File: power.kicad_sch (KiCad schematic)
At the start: 58 parts, among them J3 Conn_01x01, J4 Conn_01x01, U3 TPS53647, U36 MCP1824T-1202E, U6 AP3211, U7 MCP1824T-0802E

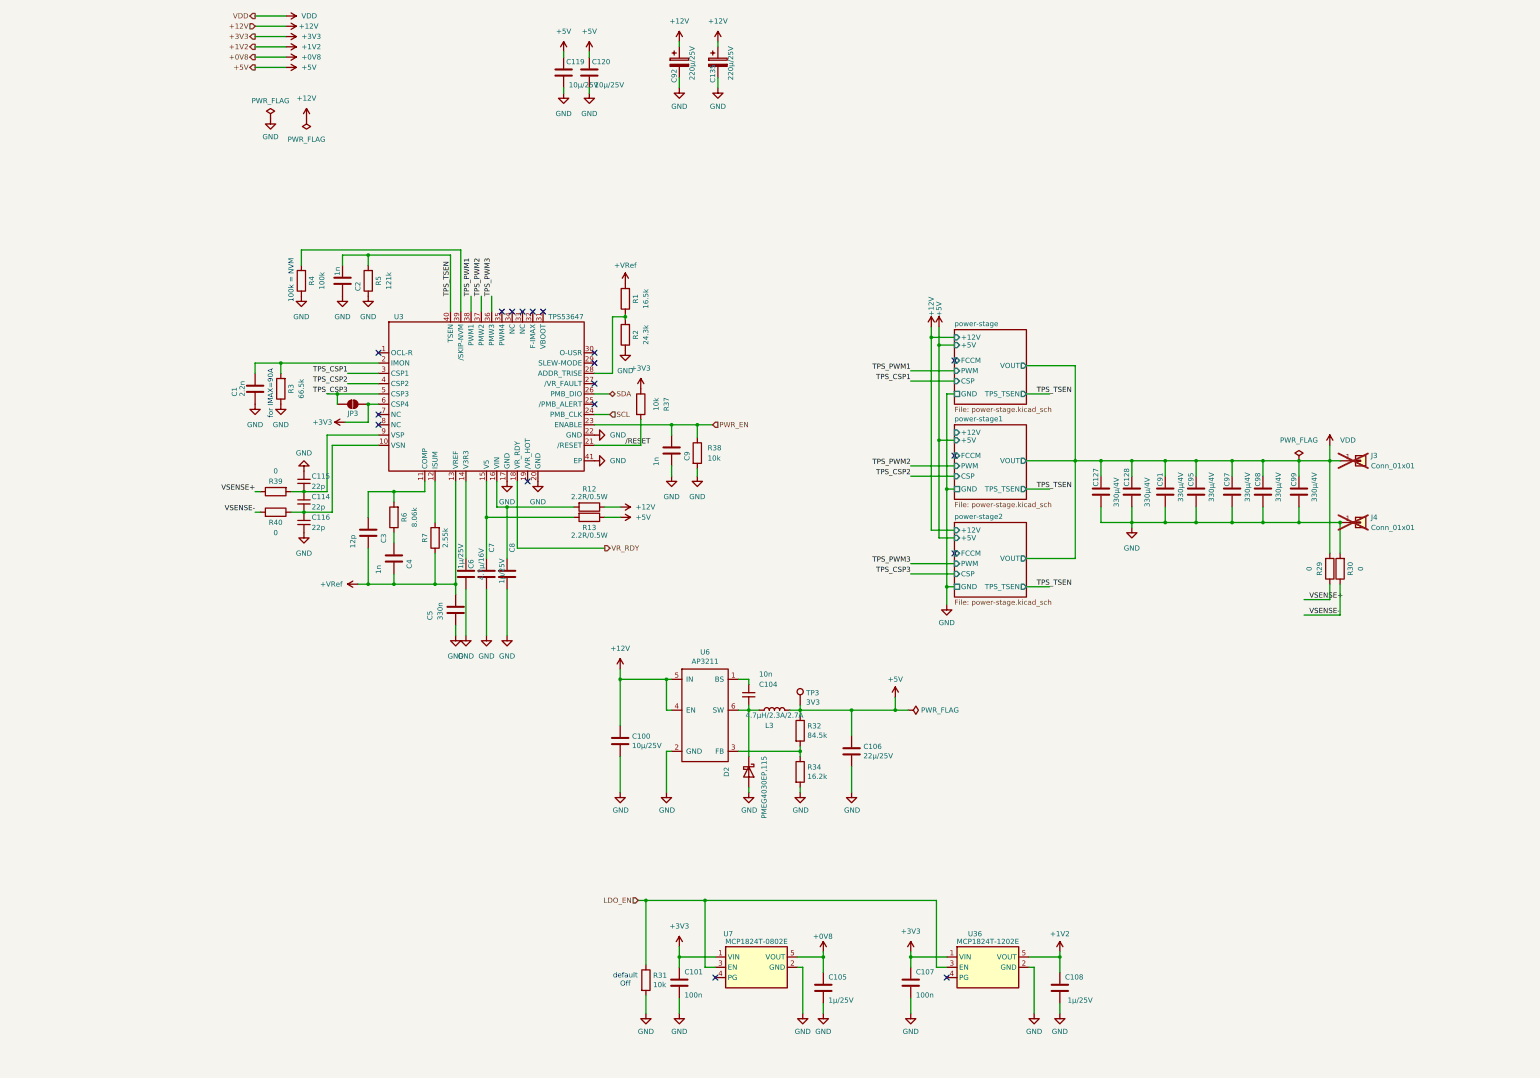
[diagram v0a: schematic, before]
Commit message: updated power stage placements
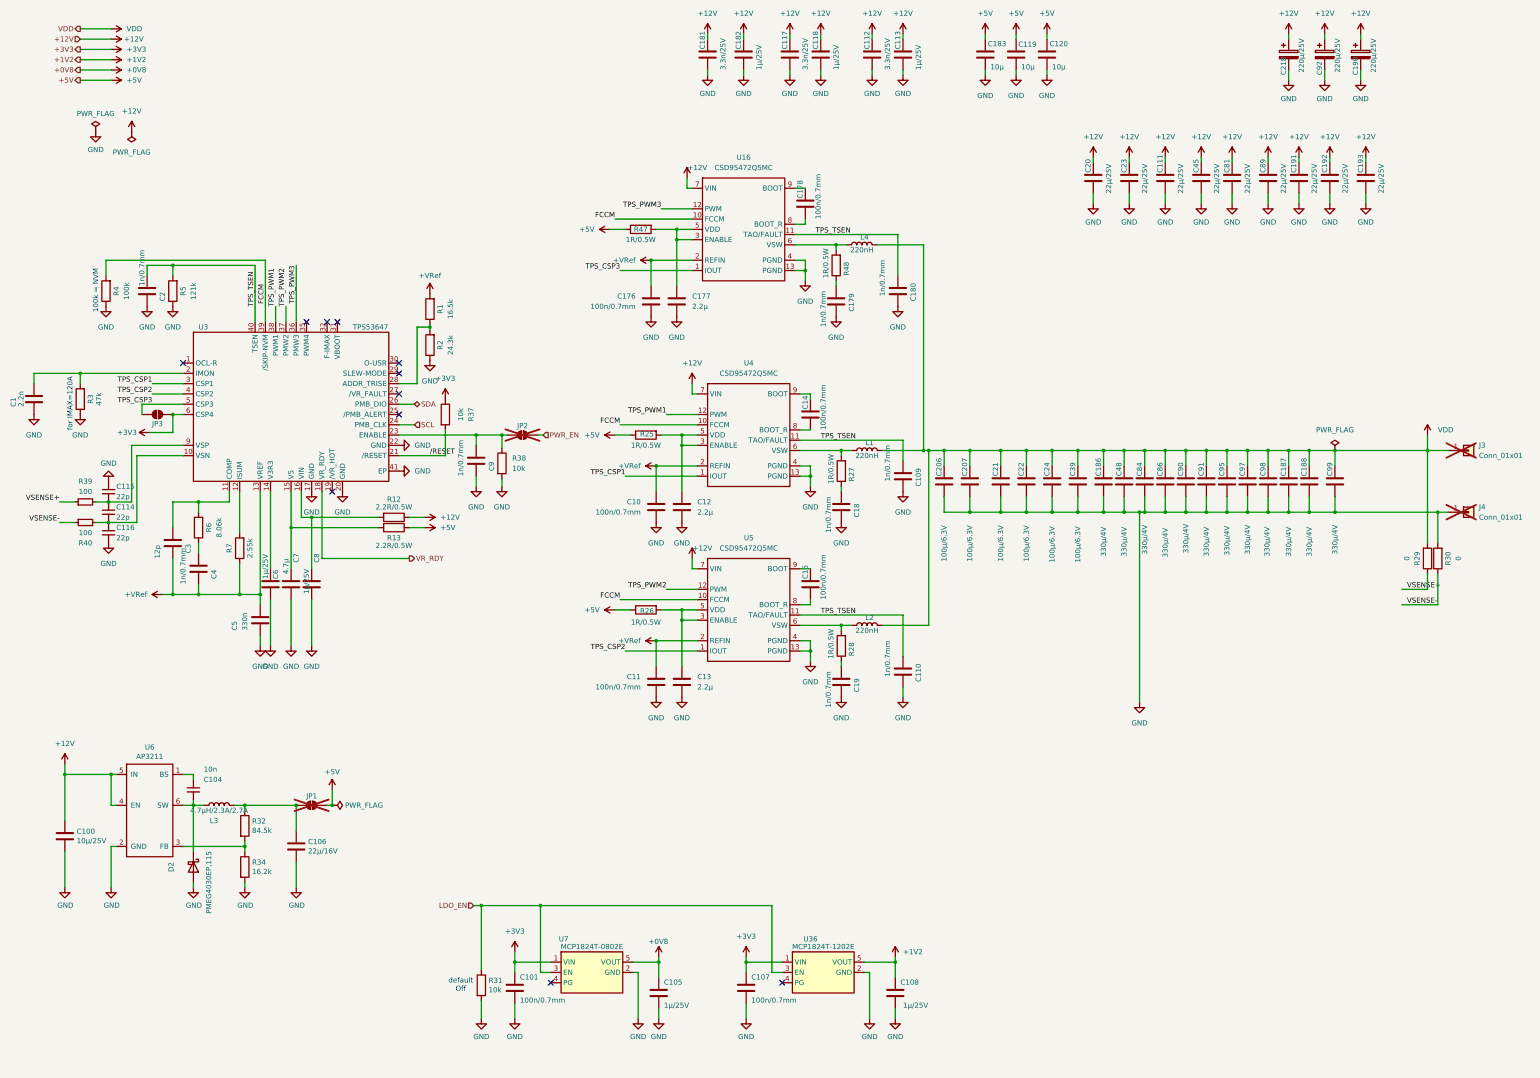
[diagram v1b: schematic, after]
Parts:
- removed C127, C128: 330µ/4V, Capacitor_SMD:C_1210_3225Metric, symbol Device:C
- removed C135: 220µ/25V, Capacitor_SMD:CP_Elec_8x10, symbol Device:C_Polarized
- removed R39, R40: 0, Resistor_SMD:R_0805_2012Metric, symbol Device:R
- removed TP3: 3V3, TestPoint:TestPoint_Pad_2.0x2.0mm, symbol Connector:TestPoint
- added C10, C11, C14, C16, C176, C178: 100n/0.7mm, Capacitor_SMD:C_0805_2012Metric, symbol Device:C
- added C109, C110, C179, C18, C180, C19: 1n/0.7mm, Capacitor_SMD:C_0805_2012Metric, symbol Device:C
- added C111, C191, C192, C193, C20, C23, C45, C81, C89: 22µ/25V, Capacitor_SMD:C_1210_3225Metric, symbol Device:C
- added C112, C117, C181: 3.3n/25V, Capacitor_SMD:C_0805_2012Metric, symbol Device:C
- added C113, C118, C182: 1µ/25V, Capacitor_SMD:C_0805_2012Metric, symbol Device:C
- added C12, C13, C177: 2.2µ, Capacitor_SMD:C_0805_2012Metric, symbol Device:C
- added C183: 10µ, Capacitor_SMD:C_0805_2012Metric, symbol Device:C
- added C186, C187, C188, C48, C84, C86, C90: 330µ/4V, Capacitor_SMD:C_1210_3225Metric, symbol Device:C
- added C190, C218: 220µ/25V, Capacitor_SMD:CP_Elec_8x10, symbol Device:C_Polarized
- added C206, C207, C21, C22, C24, C39: 100µ/6.3V, Capacitor_SMD:C_1210_3225Metric, symbol Device:C
- added JP1, JP2: SolderJumper_2_Open, Jumper:SolderJumper-2_P1.3mm_Open_RoundedPad1.0x1.5mm, symbol Jumper:SolderJumper_2_Open
- added L1, L2, L4: 220nH, Nerd8:IFLR-4031GC-01-8x10, symbol Device:L
- added R25, R26, R27, R28, R47, R48: 1R/0.5W, Resistor_SMD:R_0805_2012Metric, symbol Device:R
- added R39, R40: 100, Resistor_SMD:R_0805_2012Metric, symbol Device:R_Small
- added U16, U4, U5: CSD95472Q5MC, Nerd8:CSD95472-SON-5x6, symbol mylib7:CSD95472Q5MC
- C1: Manufacturer C0805C222J2GACTU -> CL21C222JBFNNNE; OrderNr 399-17628-1-ND -> 1276-2993-1-ND; temp-coefficient C0G -> (none)
- C100: Manufacturer GRM21BZ71E106KE15L -> C2012X5R1E106K125AB; OrderNr 490-GRM21BZ71E106KE15LCT-ND -> 445-5984-1-ND; temp-coefficient X7R -> (none)
- C101, C107: value 100n -> 100n/0.7mm; Manufacturer C0805C104K5RACTU -> AC0805KRX7R9BB104; OrderNr 399-C0805C104K5RACTUCT-ND -> 311-3037-1-ND; temp-coefficient X7R -> (none)
- C104: Manufacturer C0805C103J1GECTU -> 885012207011; OrderNr 399-C0805C103J1GECTUCT-ND -> 732-8021-1-ND; temp-coefficient C0G -> (none)
- C105, C108, C6, C8: Manufacturer CL21B105KBFNNNE -> CL21B105KAFNNNE; OrderNr 1276-1029-1-ND -> 1276-1066-1-ND; temp-coefficient X7R -> (none)
- C106: value 22µ/25V -> 22µ/16V; footprint Capacitor_SMD:C_1210_3225Metric -> Capacitor_SMD:C_1206_3216Metric; Manufacturer CL32B226KAJNNNE -> CL31A226MOCLNNC; OrderNr 1276-3392-1-ND -> 1276-2728-1-ND; temp-coefficient X7R -> (none)
- C114, C115, C116: OrderNr KGM15ACG1H220JT -> 478-KGM15ACG1H220JTCT-ND; temp-coefficient C0G -> (none)
- C119, C120: value 10µ/25V -> 10µ; Manufacturer GRM21BZ71E106KE15L -> C2012X5R1E106K125AB; OrderNr 490-GRM21BZ71E106KE15LCT-ND -> 445-5984-1-ND; temp-coefficient X7R -> (none)
- C2, C4, C9: value 1n -> 1n/0.7mm; Manufacturer C0805C102J2GECTU -> CC0805KRX7R0BB102; OrderNr 399-C0805C102J2GECTUCT-ND -> 311-1472-1-ND; temp-coefficient C0G -> (none)
- C3: OrderNr KGM15ACG2A120JM -> 478-KGM15ACG2A120JMCT-ND; temp-coefficient C0G -> (none)
- C5: Manufacturer CL21B334KBFNNNE -> C0805C334K3RECAUTO; OrderNr 1276-1123-1-ND -> 399-C0805C334K3RECAUTOCT-ND; temp-coefficient X7R -> (none)
- C7: value 4.7µ/16V -> 4.7µ; Manufacturer GRM21BR71C475KE51K -> CL21A475KAQNNNE; OrderNr 490-GRM21BR71C475KE51KCT-ND -> 1276-1244-1-ND; temp-coefficient X7R -> (none)
- C91, C95, C97, C98, C99: temp-coefficient X5R -> (none)
- C92: Manufacturer HHXE250ARA221MHA0G -> 875075355002; OrderNr 565-HHXE250ARA221MHA0GCT-ND -> 732-6489-1-ND
- R3: value 66.5k -> 47k; Manufacturer RC0805FR-0766K5L -> RMCF0805FT33K2; OrderNr 311-66.5KCRCT-ND -> RMCF0805FT33K2CT-ND
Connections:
- net +12V: now also C111.1, C112.1, C113.1, C117.1, C118.1, C181.1, C182.1, C190.1, C191.1, C192.1, C193.1, C20.1, C218.1, C23.1, C45.1, C81.1, C89.1, U16.7 (VIN), U4.7 (VIN), U5.7 (VIN)
- net +5V: now also C183.1, JP1.2 (B), R25.1, R26.1, R47.1; no longer C106.1, L3.2, R32.1
- net +VRef: now also C10.1, C11.1, C176.1, U16.2 (REFIN), U4.2 (REFIN), U5.2 (REFIN)
- net GND: now also C10.2, C109.2, C11.2, C110.2, C111.2, C112.2, C113.2, C117.2, C118.2, C12.2, C13.2, C176.2, C177.2, C179.2, C18.2, C180.2, C181.2, C182.2, C183.2, C186.2, C187.2, C188.2, C19.2, C190.2, C191.2, C192.2, C193.2, C20.2, C206.2, C207.2, C21.2, C218.2, C22.2, C23.2, C24.2, C39.2, C45.2, C48.2, C81.2, C84.2, C86.2, C89.2, C90.2, U16.13 (PGND), U16.4 (PGND), U4.13 (PGND), U4.4 (PGND), U5.13 (PGND), U5.4 (PGND)
- net PWR_EN: now also JP2.2 (B); no longer C9.1, R38.1, U3.23 (ENABLE)
- net TPS_CSP1: now also U4.1 (IOUT)
- net TPS_CSP2: now also U5.1 (IOUT)
- net TPS_CSP3: now also U16.1 (IOUT)
- net TPS_PWM1: now also U4.12 (PWM)
- net TPS_PWM2: now also U5.12 (PWM)
- net TPS_PWM3: now also U16.12 (PWM)
- net TPS_TSEN: now also C109.1, C110.1, C180.1, U16.11 (TAO/FAULT), U4.11 (TAO/FAULT), U5.11 (TAO/FAULT)
- net VDD: now also C186.1, C187.1, C188.1, C206.1, C207.1, C21.1, C22.1, C24.1, C39.1, C48.1, C84.1, C86.1, C90.1, L1.2, L2.2, L4.2
- net VSENSE+: now also R39.1
- net VSENSE-: now also R40.1
- net at C114.2, C116.1, U3.10 (VSN): now also R40.2
- net FCCM: now reaches R4.2, U3.39 (/SKIP-NVM)
- net FCCM: now also U16.10 (FCCM), U4.10 (FCCM), U5.10 (FCCM)
- net at C114.1, C115.2, U3.9 (VSP): now also R39.2
- new net: C179.1, R48.1
- new net: L4.1, R48.2, U16.6 (VSW)
- new net: C177.1, R47.2, U16.3 (ENABLE), U16.5 (VDD)
- new net: C9.1, JP2.1 (A), R38.1, U3.23 (ENABLE)
- new net: C16.1, U5.9 (BOOT)
- new net: C16.2, U5.8 (BOOT_R)
- new net: C12.1, R25.2, U4.3 (ENABLE), U4.5 (VDD)
- new net: C106.1, JP1.1 (A), L3.2, R32.1
- new net: C14.1, U4.9 (BOOT)
- new net: C14.2, U4.8 (BOOT_R)
- new net: C13.1, R26.2, U5.3 (ENABLE), U5.5 (VDD)
- new net: L2.1, R28.2, U5.6 (VSW)
- new net: C18.1, R27.1
- new net: C19.1, R28.1
- new net: L1.1, R27.2, U4.6 (VSW)
- new net: C178.1, U16.9 (BOOT)
- new net: C178.2, U16.8 (BOOT_R)
- no-connect marks 18 -> 11
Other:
- removed sheet power-stage
- removed sheet power-stage1
- removed sheet power-stage2
- note added: "for IMAX=120A"
- note removed: "for IMAX=90A"
- moved on the sheet: C1, C100, C101, C104, C105, C106, C107, C108, C114, C115, C116, C119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

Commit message: power stage in place
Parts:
- C1, C2, C4, C5, C6, C7, C8, C9: footprint Capacitor_SMD:C_0805_2012Metric -> Capacitor_SMD:C_0603_1608Metric
- R1, R2, R3, R37, R38, R39, R4, R40, R5, R6, R7: footprint Resistor_SMD:R_0805_2012Metric -> Resistor_SMD:R_0603_1608Metric
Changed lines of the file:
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@@
 			)
 		)
-		(property "Footprint" "Capacitor_SMD:C_0805_2012Metric"
+		(property "Footprint" "Capacitor_SMD:C_0603_1608Metric"
 			(at 47.2948 95.25 0)
 			(hide yes)
@@
 			)
 		)
-		(property "Footprint" "Resistor_SMD:R_0805_2012Metric"
+		(property "Footprint" "Resistor_SMD:R_0603_1608Metric"
 			(at 39.878 91.44 90)
 			(hide yes)
@@
 			)
 		)
-		(property "Footprint" "Resistor_SMD:R_0805_2012Metric"
+		(property "Footprint" "Resistor_SMD:R_0603_1608Metric"
 			(at 62.738 149.86 90)
 			(hide yes)
@@
 			)
 		)
-		(property "Footprint" "Resistor_SMD:R_0805_2012Metric"
+		(property "Footprint" "Resistor_SMD:R_0603_1608Metric"
 			(at 134.112 133.985 90)
 			(hide yes)
@@
 			)
 		)
-		(property "Footprint" "Resistor_SMD:R_0805_2012Metric"
+		(property "Footprint" "Resistor_SMD:R_0603_1608Metric"
 			(at 119.888 95.885 90)
 			(hide yes)
@@
 			)
 		)
-		(property "Footprint" "Capacitor_SMD:C_0805_2012Metric"
+		(property "Footprint" "Capacitor_SMD:C_0603_1608Metric"
 			(at 128.5748 137.16 0)
 			(hide yes)
@@
 			)
 		)
-		(property "Footprint" "Capacitor_SMD:C_0805_2012Metric"
+		(property "Footprint" "Capacitor_SMD:C_0603_1608Metric"
 			(at 77.7748 167.64 0)
 			(hide yes)
@@
 			)
 		)
-		(property "Footprint" "Resistor_SMD:R_0805_2012Metric"
+		(property "Footprint" "Resistor_SMD:R_0603_1608Metric"
 			(at 33.02 143.51 0)
 			(hide yes)
@@
 			)
 		)
-		(property "Footprint" "Capacitor_SMD:C_0805_2012Metric"
+		(property "Footprint" "Capacitor_SMD:C_0603_1608Metric"
 			(at 59.9948 163.83 0)
 			(hide yes)
@@
 			)
 		)
-		(property "Footprint" "Capacitor_SMD:C_0805_2012Metric"
+		(property "Footprint" "Capacitor_SMD:C_0603_1608Metric"
 			(at 82.8548 160.02 0)
 			(hide yes)
@@
 			)
 		)
-		(property "Footprint" "Capacitor_SMD:C_0805_2012Metric"
+		(property "Footprint" "Capacitor_SMD:C_0603_1608Metric"
 			(at 75.2348 176.53 0)
 			(hide yes)
@@
 			)
 		)
-		(property "Footprint" "Resistor_SMD:R_0805_2012Metric"
+		(property "Footprint" "Resistor_SMD:R_0603_1608Metric"
 			(at 119.888 104.775 90)
 			(hide yes)
@@
 			)
 		)
-		(property "Footprint" "Resistor_SMD:R_0805_2012Metric"
+		(property "Footprint" "Resistor_SMD:R_0603_1608Metric"
 			(at 33.528 118.11 90)
 			(hide yes)
@@
 			)
 		)
-		(property "Footprint" "Capacitor_SMD:C_0805_2012Metric"
+		(property "Footprint" "Capacitor_SMD:C_0603_1608Metric"
 			(at 19.3548 121.92 0)
 			(hide yes)
@@
 			)
 		)
-		(property "Footprint" "Resistor_SMD:R_0805_2012Metric"
+		(property "Footprint" "Resistor_SMD:R_0603_1608Metric"
 			(at 33.02 148.59 0)
 			(hide yes)
@@
 			)
 		)
-		(property "Footprint" "Resistor_SMD:R_0805_2012Metric"
+		(property "Footprint" "Resistor_SMD:R_0603_1608Metric"
 			(at 120.142 121.92 90)
 			(hide yes)
@@
 			)
 		)
-		(property "Footprint" "Resistor_SMD:R_0805_2012Metric"
+		(property "Footprint" "Resistor_SMD:R_0603_1608Metric"
 			(at 72.898 154.94 90)
 			(hide yes)
@@
 			)
 		)
-		(property "Footprint" "Resistor_SMD:R_0805_2012Metric"
+		(property "Footprint" "Resistor_SMD:R_0603_1608Metric"
 			(at 56.388 91.44 90)
 			(hide yes)
@@
 			)
 		)
-		(property "Footprint" "Capacitor_SMD:C_0805_2012Metric"
+		(property "Footprint" "Capacitor_SMD:C_0603_1608Metric"
 			(at 87.9348 160.02 0)
 			(hide yes)

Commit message: shrinking layout to fit
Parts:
- C14, C16, C178: footprint Capacitor_SMD:C_0805_2012Metric -> Capacitor_SMD:C_0603_1608Metric
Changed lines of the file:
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@@
 			)
 		)
-		(property "Footprint" "Capacitor_SMD:C_0805_2012Metric"
+		(property "Footprint" "Capacitor_SMD:C_0603_1608Metric"
 			(at 213.0552 167.64 0)
 			(hide yes)
@@
 			)
 		)
-		(property "Footprint" "Capacitor_SMD:C_0805_2012Metric"
+		(property "Footprint" "Capacitor_SMD:C_0603_1608Metric"
 			(at 213.0552 125.73 0)
 			(hide yes)
@@
 			)
 		)
-		(property "Footprint" "Capacitor_SMD:C_0805_2012Metric"
+		(property "Footprint" "Capacitor_SMD:C_0603_1608Metric"
 			(at 211.7852 73.66 0)
 			(hide yes)

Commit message: optimizing pwr stage placement
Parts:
- C10, C11, C112, C113, C117, C118, C12, C13, C176, C177, C181, C182: footprint Capacitor_SMD:C_0805_2012Metric -> Capacitor_SMD:C_0603_1608Metric
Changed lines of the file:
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@@
 			)
 		)
-		(property "Footprint" "Capacitor_SMD:C_0805_2012Metric"
+		(property "Footprint" "Capacitor_SMD:C_0603_1608Metric"
 			(at 180.0352 97.79 0)
 			(hide yes)
@@
 			)
 		)
-		(property "Footprint" "Capacitor_SMD:C_0805_2012Metric"
+		(property "Footprint" "Capacitor_SMD:C_0603_1608Metric"
 			(at 173.0248 148.59 0)
 			(hide yes)
@@
 			)
 		)
-		(property "Footprint" "Capacitor_SMD:C_0805_2012Metric"
+		(property "Footprint" "Capacitor_SMD:C_0603_1608Metric"
 			(at 181.3052 148.59 0)
 			(hide yes)
@@
 			)
 		)
-		(property "Footprint" "Capacitor_SMD:C_0805_2012Metric"
+		(property "Footprint" "Capacitor_SMD:C_0603_1608Metric"
 			(at 171.7548 97.79 0)
 			(hide yes)
@@
 			)
 		)
-		(property "Footprint" "Capacitor_SMD:C_0805_2012Metric"
+		(property "Footprint" "Capacitor_SMD:C_0603_1608Metric"
 			(at 173.0248 191.77 0)
 			(hide yes)
@@
 			)
 		)
-		(property "Footprint" "Capacitor_SMD:C_0805_2012Metric"
+		(property "Footprint" "Capacitor_SMD:C_0603_1608Metric"
 			(at 181.3052 191.77 0)
 			(hide yes)
@@
 			)
 		)
-		(property "Footprint" "Capacitor_SMD:C_0805_2012Metric"
+		(property "Footprint" "Capacitor_SMD:C_0603_1608Metric"
 			(at 196.5452 36.83 0)
 			(hide yes)
@@
 			)
 		)
-		(property "Footprint" "Capacitor_SMD:C_0805_2012Metric"
+		(property "Footprint" "Capacitor_SMD:C_0603_1608Metric"
 			(at 187.6552 36.83 0)
 			(hide yes)
@@
 			)
 		)
-		(property "Footprint" "Capacitor_SMD:C_0805_2012Metric"
+		(property "Footprint" "Capacitor_SMD:C_0603_1608Metric"
 			(at 207.9752 36.83 0)
 			(hide yes)
@@
 			)
 		)
-		(property "Footprint" "Capacitor_SMD:C_0805_2012Metric"
+		(property "Footprint" "Capacitor_SMD:C_0603_1608Metric"
 			(at 215.5952 36.83 0)
 			(hide yes)
@@
 			)
 		)
-		(property "Footprint" "Capacitor_SMD:C_0805_2012Metric"
+		(property "Footprint" "Capacitor_SMD:C_0603_1608Metric"
 			(at 228.2952 36.83 0)
 			(hide yes)
@@
 			)
 		)
-		(property "Footprint" "Capacitor_SMD:C_0805_2012Metric"
+		(property "Footprint" "Capacitor_SMD:C_0603_1608Metric"
 			(at 235.9152 36.83 0)
 			(hide yes)

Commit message: DC stage close to LGA socket
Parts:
- removed C218: 220µ/25V, Capacitor_SMD:CP_Elec_8x10, symbol Device:C_Polarized

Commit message: sch_ should be ready
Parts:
- removed JP1: SolderJumper_2_Open, Jumper:SolderJumper-2_P1.3mm_Open_RoundedPad1.0x1.5mm, symbol Jumper:SolderJumper_2_Open
- added C102: 10µ/25V, Capacitor_SMD:C_0805_2012Metric, symbol Device:C
- added C151: 10n, Capacitor_SMD:C_0805_2012Metric, symbol Device:C_Small
- added C152: 22µ/16V, Capacitor_SMD:C_1206_3216Metric, symbol Device:C
- added D6: PMEG4030EP,115, Diode_SMD:D_SOD-128, symbol Device:D_Schottky
- added L6: 4.7µH/2.3A/2.7A, Inductor_SMD:L_Taiyo-Yuden_NR-50xx, symbol Device:L
- added R69: 49.9k, Resistor_SMD:R_0603_1608Metric, symbol Device:R
- added R70: 16.2k, Resistor_SMD:R_0603_1608Metric, symbol Device:R
- added U14: AP3211, Package_TO_SOT_SMD:SOT-23-6, symbol pferdibank-rescue:AP3211-mylib
- R32, R34: footprint Resistor_SMD:R_0805_2012Metric -> Resistor_SMD:R_0603_1608Metric
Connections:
- net +12V: now also C102.1, U14.4 (EN), U14.5 (IN)
- net +3V3: now also C152.1, L6.2, R69.1
- net +5V: now also C106.1, L3.2, R32.1
- net GND: now also C102.2, C152.2, D6.2 (A), R70.2, U14.2 (GND)
- new net: C151.1, U14.1 (BS)
- new net: R69.2, R70.1, U14.3 (FB)
- new net: C151.2, D6.1 (K), L6.1, U14.6 (SW)
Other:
- moved on the sheet: C100, C104, C106, D2, L3, R32, R34, U6
